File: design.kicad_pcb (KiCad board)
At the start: 2 copper layers, 28.5 x 12 mm, 5 parts, among them J1 USB_C_Receptacle, J2 Conn_01x05, U1 ATtiny1616-M

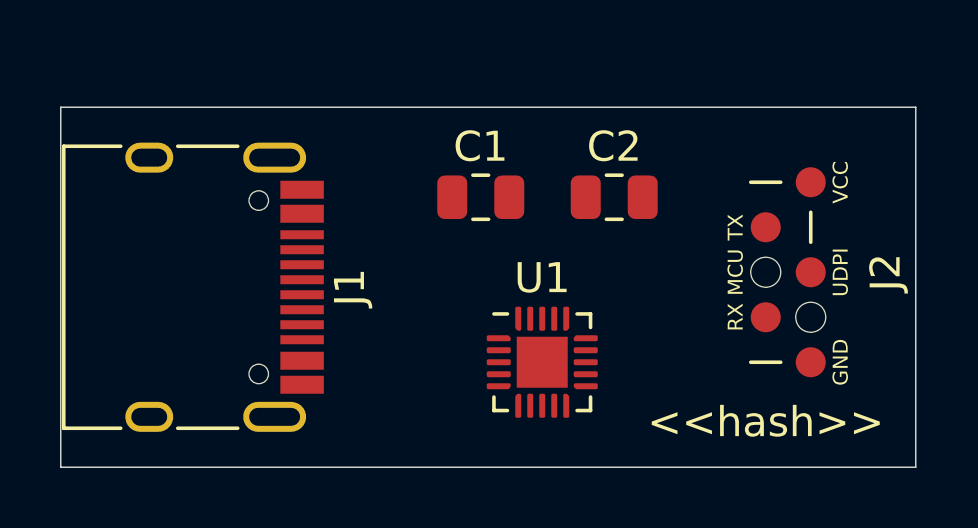
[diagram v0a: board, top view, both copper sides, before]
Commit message: convert to KiCad 6
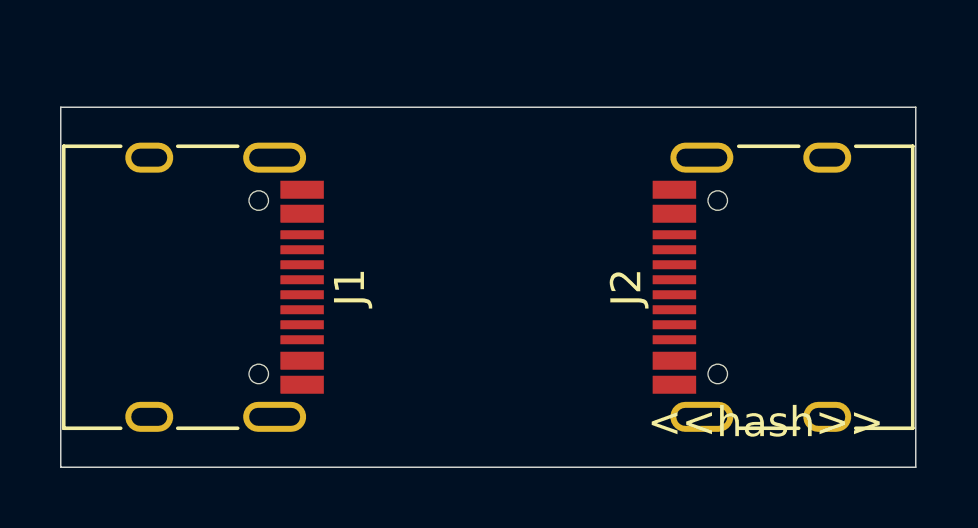
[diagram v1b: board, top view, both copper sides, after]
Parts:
- removed C1, C2: C_Small, Capacitor_SMD:C_0805_2012Metric
- removed U1: ATtiny1616-M, Package_DFN_QFN:VQFN-20-1EP_3x3mm_P0.4mm_EP1.7x1.7mm
- J2: value Conn_01x05 -> USB_C_Receptacle; footprint E32-xxxT20D:UDPI_interface -> Connector_USB:USB_C_Receptacle_HRO_TYPE-C-31-M-12
- moved J2 0.71 mm to (161.0, 86.0), turned to 90 degrees
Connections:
- net Net-(J1-PadA1) renamed GND
- net Net-(J1-PadA4) renamed VCC
- J1 pad A6: Net-(J1-PadA6) -> D+
- J1 pad A7: Net-(J1-PadA7) -> D-
- J1 pad A8: Net-(J1-PadA8) -> unconnected-(J1-PadA8)
- J1 pad B6: Net-(J1-PadB6) -> D+
- J1 pad B7: Net-(J1-PadB7) -> D-
- J1 pad B8: Net-(J1-PadB8) -> unconnected-(J1-PadB8)
- J1 pad S1: Net-(J1-PadS1) -> unconnected-(J1-PadS1)
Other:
- net class Default removed

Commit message: ?
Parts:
- added J3: Conn_01x03, Connector:Pogo-Pin-01x03_2.54, F.Cu at (151.0, 82.0)
- added R1: R_Small, Resistor_SMD:R_0805_2012Metric, F.Cu at (149.2, 86.3)
- added R2: R_Small, Resistor_SMD:R_0805_2012Metric, F.Cu at (149.0, 89.0)
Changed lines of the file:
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@@
   (net 19 "Net-(J2-PadA1)")
   (net 20 "Net-(J2-PadA4)")
+  (net 21 "unconnected-(J3-Pad1)")
+  (net 22 "unconnected-(J3-Pad2)")
+  (net 23 "unconnected-(J3-Pad3)")
   (footprint "Connector_USB:USB_C_Receptacle_HRO_TYPE-C-31-M-12" (layer "F.Cu")
     (at 140.5 86 -90)
@@
     )
   )
+  (footprint "Connector:Pogo-Pin-01x03_2.54" (layer "F.Cu")
+    (at 151 82)
+    (property "Sheetfile" "/Users/tobias/Documents/GitHub/UPDI-Programmer/design.sch")
+    (property "Sheetname" "")
+    (attr smd)
+    (fp_text reference "J3" (at 0 -2.54 unlocked) (layer "F.SilkS")
+      (effects (font (size 1 1) (thickness 0.15)))
+    )
+    (fp_text value "Conn_01x03" (at 0 2.54 unlocked) (layer "F.Fab")
+      (effects (font (size 1 1) (thickness 0.15)))
+    )
+    (fp_text user "${REFERENCE}" (at 0 5.08 unlocked) (layer "F.Fab")
+      (effects (font (size 1 1) (thickness 0.15)))
+    )
+    (pad "1" smd circle (at 0 0) (size 2 2) (layers "F.Cu" "F.Paste" "F.Mask")
+      (net 21 "unconnected-(J3-Pad1)") (pinfunction "Pin_1") (pintype "passive"))
+    (pad "2" smd circle (at 2.54 0) (size 2 2) (layers "F.Cu" "F.Paste" "F.Mask")
+      (net 22 "unconnected-(J3-Pad2)") (pinfunction "Pin_2") (pintype "passive"))
+    (pad "3" smd circle (at -2.54 0) (size 2 2) (layers "F.Cu" "F.Paste" "F.Mask")
+      (net 23 "unconnected-(J3-Pad3)") (pinfunction "Pin_3") (pintype "passive"))
+  )
+  (footprint "Resistor_SMD:R_0805_2012Metric" (layer "F.Cu")
+    (at 149.185 86.305)
+    (descr "Resistor SMD 0805 (2012 Metric), square (rectangular) end terminal, IPC_7351 nominal, (Body size source: IPC-SM-782 page 72, https://www.pcb-3d.com/wordpress/wp-content/uploads/ipc-sm-782a_amendment_1_and_2.pdf), generated with kicad-footprint-generator")
+    (tags "resistor")
+    (property "Sheetfile" "/Users/tobias/Documents/GitHub/UPDI-Programmer/design.sch")
+    (property "Sheetname" "")
+    (attr smd)
+    (fp_text reference "R1" (at 0 -1.65) (layer "F.SilkS")
+      (effects (font (size 1 1) (thickness 0.15)))
+    )
+    (fp_text value "R_Small" (at 0 1.65) (layer "F.Fab")
+      (effects (font (size 1 1) (thickness 0.15)))
+    )
+    (fp_text user "${REFERENCE}" (at 0 0) (layer "F.Fab")
+      (effects (font (size 0.5 0.5) (thickness 0.08)))
+    )
+    (fp_line (start -0.227064 0.735) (end 0.227064 0.735) (layer "F.SilkS") (width 0.12))
+    (fp_line (start -0.227064 -0.735) (end 0.227064 -0.735) (layer "F.SilkS") (width 0.12))
+    (fp_line (start -1.68 0.95) (end -1.68 -0.95) (layer "F.CrtYd") (width 0.05))
+    (fp_line (start 1.68 0.95) (end -1.68 0.95) (layer "F.CrtYd") (width 0.05))
+    (fp_line (start 1.68 -0.95) (end 1.68 0.95) (layer "F.CrtYd") (width 0.05))
+    (fp_line (start -1.68 -0.95) (end 1.68 -0.95) (layer "F.CrtYd") (width 0.05))
+    (fp_line (start 1 0.625) (end -1 0.625) (layer "F.Fab") (width 0.1))
+    (fp_line (start 1 -0.625) (end 1 0.625) (layer "F.Fab") (width 0.1))
+    (fp_line (start -1 0.625) (end -1 -0.625) (layer "F.Fab") (width 0.1))
+    (fp_line (start -1 -0.625) (end 1 -0.625) (layer "F.Fab") (width 0.1))
+    (pad "1" smd roundrect locked (at -0.9125 0) (size 1.025 1.4) (layers "F.Cu" "F.Paste" "F.Mask") (roundrect_rratio 0.243902)
+      (net 1 "GND") (pintype "passive"))
+    (pad "2" smd roundrect locked (at 0.9125 0) (size 1.025 1.4) (layers "F.Cu" "F.Paste" "F.Mask") (roundrect_rratio 0.243902)
+      (net 8 "Net-(J1-PadA5)") (pintype "passive"))
+    (model "${KICAD6_3DMODEL_DIR}/Resistor_SMD.3dshapes/R_0805_2012Metric.wrl"
+      (offset (xyz 0 0 0))
+      (scale (xyz 1 1 1))
+      (rotate (xyz 0 0 0))
+    )
+  )
+  (footprint "Resistor_SMD:R_0805_2012Metric" (layer "F.Cu")
+    (at 149 89)
+    (descr "Resistor SMD 0805 (2012 Metric), square (rectangular) end terminal, IPC_7351 nominal, (Body size source: IPC-SM-782 page 72, https://www.pcb-3d.com/wordpress/wp-content/uploads/ipc-sm-782a_amendment_1_and_2.pdf), generated with kicad-footprint-generator")
+    (tags "resistor")
+    (property "Sheetfile" "/Users/tobias/Documents/GitHub/UPDI-Programmer/design.sch")
+    (property "Sheetname" "")
+    (attr smd)
+    (fp_text reference "R2" (at 0 -1.65) (layer "F.SilkS")
+      (effects (font (size 1 1) (thickness 0.15)))
+    )
+    (fp_text value "R_Small" (at 0 1.65) (layer "F.Fab")
+      (effects (font (size 1 1) (thickness 0.15)))
+    )
+    (fp_text user "${REFERENCE}" (at 0 0) (layer "F.Fab")
+      (effects (font (size 0.5 0.5) (thickness 0.08)))
+    )
+    (fp_line (start -0.227064 0.735) (end 0.227064 0.735) (layer "F.SilkS") (width 0.12))
+    (fp_line (start -0.227064 -0.735) (end 0.227064 -0.735) (layer "F.SilkS") (width 0.12))
+    (fp_line (start 1.68 0.95) (end -1.68 0.95) (layer "F.CrtYd") (width 0.05))
+    (fp_line (start -1.68 0.95) (end -1.68 -0.95) (layer "F.CrtYd") (width 0.05))
+    (fp_line (start 1.68 -0.95) (end 1.68 0.95) (layer "F.CrtYd") (width 0.05))
+    (fp_line (start -1.68 -0.95) (end 1.68 -0.95) (layer "F.CrtYd") (width 0.05))
+    (fp_line (start -1 0.625) (end -1 -0.625) (layer "F.Fab") (width 0.1))
+    (fp_line (start 1 -0.625) (end 1 0.625) (layer "F.Fab") (width 0.1))
+    (fp_line (start -1 -0.625) (end 1 -0.625) (layer "F.Fab") (width 0.1))
+    (fp_line (start 1 0.625) (end -1 0.625) (layer "F.Fab") (width 0.1))
+    (pad "1" smd roundrect locked (at -0.9125 0) (size 1.025 1.4) (layers "F.Cu" "F.Paste" "F.Mask") (roundrect_rratio 0.243902)
+      (net 1 "GND") (pintype "passive"))
+    (pad "2" smd roundrect locked (at 0.9125 0) (size 1.025 1.4) (layers "F.Cu" "F.Paste" "F.Mask") (roundrect_rratio 0.243902)
+      (net 13 "Net-(J1-PadB5)") (pintype "passive"))
+    (model "${KICAD6_3DMODEL_DIR}/Resistor_SMD.3dshapes/R_0805_2012Metric.wrl"
+      (offset (xyz 0 0 0))
+      (scale (xyz 1 1 1))
+      (rotate (xyz 0 0 0))
+    )
+  )
